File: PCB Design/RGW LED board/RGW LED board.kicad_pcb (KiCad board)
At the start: 2 copper layers, 148.6 x 22 mm, 13 parts, among them J1 R strip, J10 G strip, J11 W strip, J12 R strip, J13 G strip, J2 G strip, J3 R from above, J4 W strip, J5 G from above, J6 W from above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

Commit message: Zachary IR and RGW LED boards revisions
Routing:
- net /W-: track 101.3 -> 98.7 mm
- net /G+: track 156.5 -> 158.7 mm
- net /R+: track 155.4 -> 153.6 mm

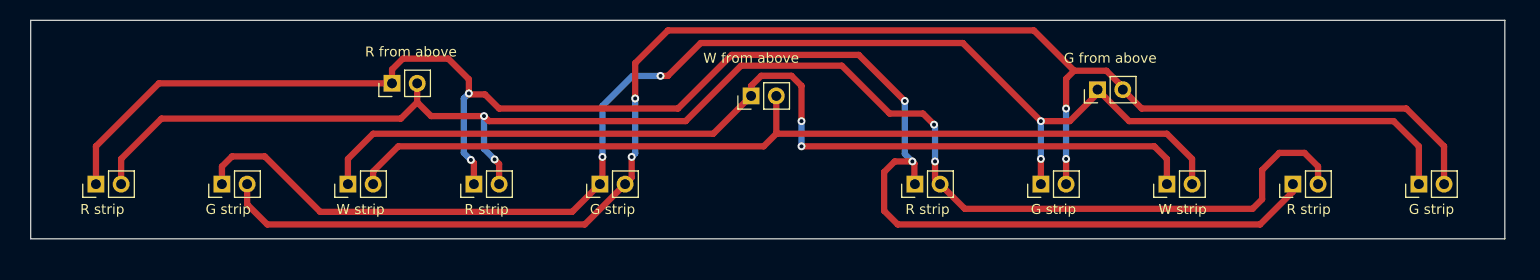
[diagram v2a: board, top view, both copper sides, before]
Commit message: Logos and labels
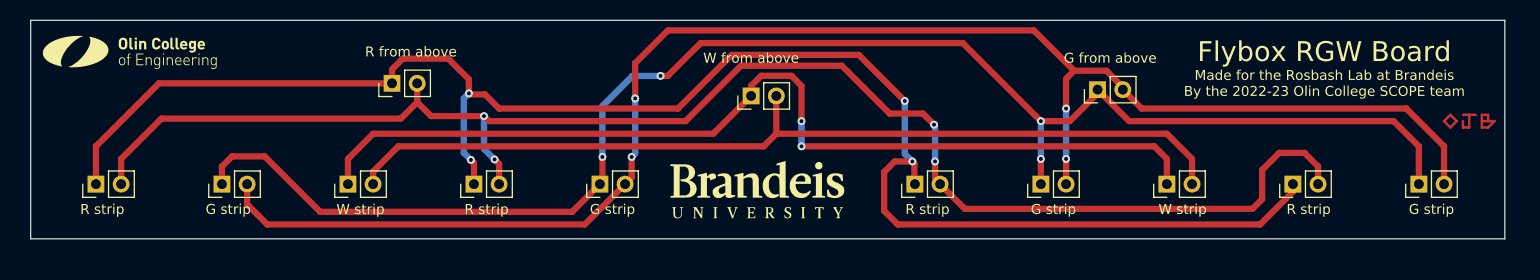
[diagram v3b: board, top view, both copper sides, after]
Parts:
- added G***: LOGO, LOGO, F.Cu at (136.5, 43.8)
- added G***: LOGO, LOGO, F.Cu at (73.0, 29.8)
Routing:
- net (no net): track 0.00 -> 12.7 mm
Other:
- board text added: "Flybox RGW Board"
- board text added: "Made for the Rosbash Lab at Brandeis By the 2022-23 Olin College SCOPE team"

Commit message: V2 IR and RGW boards done
Main board missing button footprint
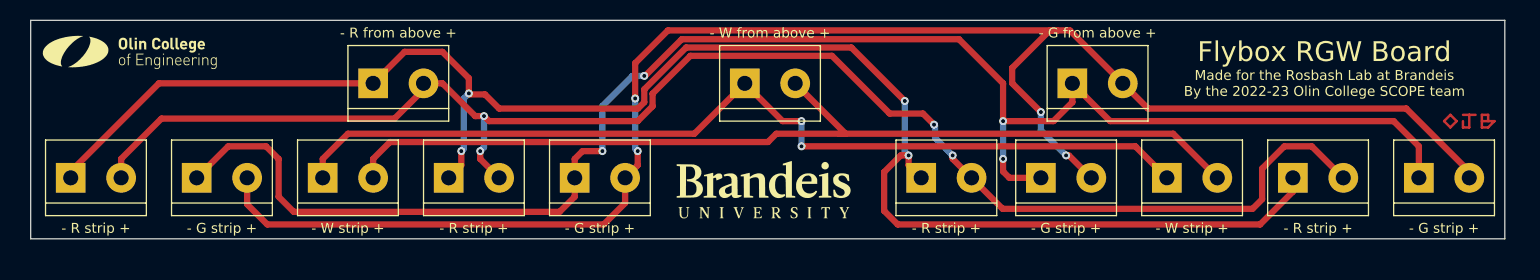
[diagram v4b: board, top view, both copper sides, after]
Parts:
- J1, J12, J7, J9: value R strip -> - R strip +; footprint Connector_PinHeader_2.54mm:PinHeader_1x02_P2.54mm_Vertical -> TerminalBlock:TerminalBlock_bornier-2_P5.08mm
- J10, J13, J2, J8: value G strip -> - G strip +; footprint Connector_PinHeader_2.54mm:PinHeader_1x02_P2.54mm_Vertical -> TerminalBlock:TerminalBlock_bornier-2_P5.08mm
- J11, J4: value W strip -> - W strip +; footprint Connector_PinHeader_2.54mm:PinHeader_1x02_P2.54mm_Vertical -> TerminalBlock:TerminalBlock_bornier-2_P5.08mm
- J3: value R from above -> - R from above +; footprint Connector_PinHeader_2.54mm:PinHeader_1x02_P2.54mm_Vertical -> TerminalBlock:TerminalBlock_bornier-2_P5.08mm
- J5: value G from above -> - G from above +; footprint Connector_PinHeader_2.54mm:PinHeader_1x02_P2.54mm_Vertical -> TerminalBlock:TerminalBlock_bornier-2_P5.08mm
- J6: value W from above -> - W from above +; footprint Connector_PinHeader_2.54mm:PinHeader_1x02_P2.54mm_Vertical -> TerminalBlock:TerminalBlock_bornier-2_P5.08mm
- moved J1 2.62 mm to (105.4, 42.5), turned to 0 degrees
- moved J10 2.62 mm to (118.1, 42.5), turned to 0 degrees
- moved J11 2.62 mm to (92.7, 42.5), turned to 0 degrees
- moved J13 2.62 mm to (80.0, 42.5), turned to 0 degrees
- moved J5 2.62 mm to (168.3, 33.0), turned to 0 degrees
- moved J9 2.62 mm to (67.3, 42.5), turned to 0 degrees
- moved J3 1.90 mm to (97.8, 33.0), turned to 0 degrees
- moved J6 1.42 mm to (135.3, 33.0), turned to 0 degrees
- moved J7 0.90 mm to (153.0, 42.5), turned to 0 degrees
- moved J12 0.63 mm to (190.5, 42.5), turned to 0 degrees
- moved J2 0.63 mm to (203.2, 42.5), turned to 0 degrees
- moved J4 0.63 mm to (177.8, 42.5), turned to 0 degrees
- moved J8 0.63 mm to (165.1, 42.5), turned to 0 degrees
- moved G*** 0.63 mm to (137.2, 43.8)
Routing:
- net /G+: track 158.7 -> 169.9 mm
- net /G-: track 154.0 -> 164.9 mm
- net /W+: track 92.8 -> 97.7 mm
- net /W-: track 98.7 -> 95.6 mm
- net /R-: track 166.7 -> 167.9 mm

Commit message: Finished V2 PCBs with rounded edges
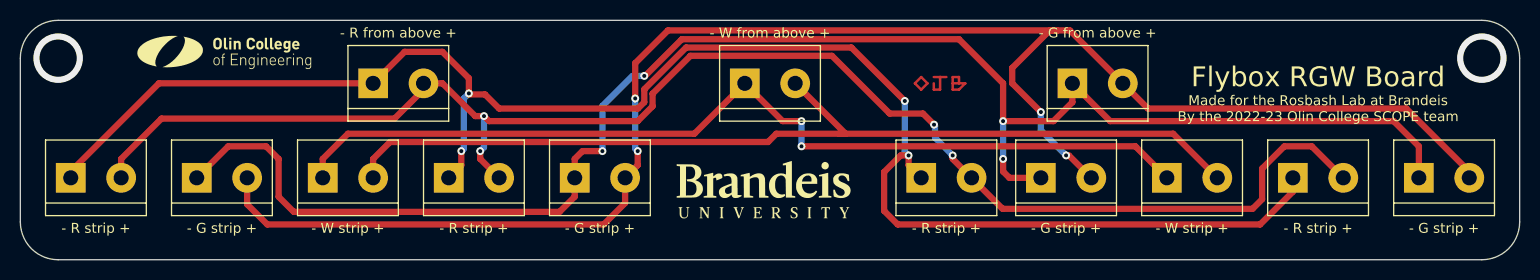
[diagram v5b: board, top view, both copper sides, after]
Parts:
- moved G*** 9.52 mm to (82.5, 29.8)
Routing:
- net (no net): vias 0 -> 2
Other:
- board size 148.6 x 22 mm -> 151.1 x 24.1 mm
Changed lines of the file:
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@@
   )
   (footprint "LOGO" (layer "F.Cu")
-    (at 73.025 29.845)
+    (at 82.55 29.845)
     (attr board_only exclude_from_pos_files exclude_from_bom)
     (fp_text reference "G***" (at 0 -1.905) (layer "F.Fab")
@@
     )
   )
-  (gr_rect (start 63.2714 26.67) (end 211.8614 48.6918) (layer "Edge.Cuts") (width 0.1) (fill none))
-  (gr_text "Made for the Rosbash Lab at Brandeis\nBy the 2022-23 Olin College SCOPE team" (at 193.675 33.02) (layer "F.SilkS")
+  (gr_arc (start 62.23 30.48) (mid 63.345923 27.785923) (end 66.04 26.67) (layer "Edge.Cuts") (width 0.1))
+  (gr_line (start 66.04 50.8) (end 209.55 50.8) (layer "Edge.Cuts") (width 0.1))
+  (gr_line (start 209.55 26.67) (end 66.04 26.67) (layer "Edge.Cuts") (width 0.1))
+  (gr_arc (start 209.55 26.67) (mid 212.244077 27.785923) (end 213.36 30.48) (layer "Edge.Cuts") (width 0.1))
+  (gr_arc (start 66.04 50.8) (mid 63.345923 49.684077) (end 62.23 46.99) (layer "Edge.Cuts") (width 0.1))
+  (gr_line (start 62.23 30.48) (end 62.23 46.99) (layer "Edge.Cuts") (width 0.1))
+  (gr_line (start 213.36 46.99) (end 213.36 30.48) (layer "Edge.Cuts") (width 0.1))
+  (gr_arc (start 213.36 46.99) (mid 212.244077 49.684077) (end 209.55 50.8) (layer "Edge.Cuts") (width 0.1))
+  (gr_rect (start 62.23 26.67) (end 213.36 50.8) (layer "F.Fab") (width 0.1) (fill none))
+  (gr_text "Made for the Rosbash Lab at Brandeis\nBy the 2022-23 Olin College SCOPE team" (at 193.04 35.56) (layer "F.SilkS")
     (effects (font (size 1 1) (thickness 0.2)))
   )
-  (gr_text "Flybox RGW Board\n" (at 193.675 29.845) (layer "F.SilkS")
+  (gr_text "Flybox RGW Board\n" (at 193.04 32.385) (layer "F.SilkS")
     (effects (font (size 2 2) (thickness 0.2)))
   )
-  (segment (start 210.82 36.83) (end 209.55 36.83) (width 0.25) (layer "F.Cu") (net 0))
-  (segment (start 210.185 36.195) (end 210.185 36.83) (width 0.25) (layer "F.Cu") (net 0))
-  (segment (start 207.645 36.195) (end 208.28 36.195) (width 0.25) (layer "F.Cu") (net 0))
-  (segment (start 209.55 36.195) (end 209.55 37.465) (width 0.25) (layer "F.Cu") (net 0))
-  (segment (start 207.01 36.83) (end 206.375 37.465) (width 0.25) (layer "F.Cu") (net 0))
-  (segment (start 205.74 36.83) (end 206.375 36.195) (width 0.25) (layer "F.Cu") (net 0))
-  (segment (start 207.645 37.465) (end 207.645 36.83) (width 0.25) (layer "F.Cu") (net 0))
-  (segment (start 209.55 37.465) (end 210.185 37.465) (width 0.25) (layer "F.Cu") (net 0))
-  (segment (start 206.375 36.195) (end 207.01 36.83) (width 0.25) (layer "F.Cu") (net 0))
-  (segment (start 210.185 37.465) (end 210.82 36.83) (width 0.25) (layer "F.Cu") (net 0))
-  (segment (start 208.28 36.195) (end 208.28 37.465) (width 0.25) (layer "F.Cu") (net 0))
-  (segment (start 209.55 36.195) (end 210.185 36.195) (width 0.25) (layer "F.Cu") (net 0))
-  (segment (start 206.375 37.465) (end 205.74 36.83) (width 0.25) (layer "F.Cu") (net 0))
-  (segment (start 208.28 37.465) (end 207.645 37.465) (width 0.25) (layer "F.Cu") (net 0))
-  (segment (start 208.28 36.195) (end 208.915 36.195) (width 0.25) (layer "F.Cu") (net 0))
+  (segment (start 157.48 33.02) (end 156.21 33.02) (width 0.25) (layer "F.Cu") (net 0))
+  (segment (start 156.845 32.385) (end 156.845 33.02) (width 0.25) (layer "F.Cu") (net 0))
+  (segment (start 154.305 32.385) (end 154.94 32.385) (width 0.25) (layer "F.Cu") (net 0))
+  (segment (start 156.21 32.385) (end 156.21 33.655) (width 0.25) (layer "F.Cu") (net 0))
+  (segment (start 153.67 33.02) (end 153.035 33.655) (width 0.25) (layer "F.Cu") (net 0))
+  (segment (start 152.4 33.02) (end 153.035 32.385) (width 0.25) (layer "F.Cu") (net 0))
+  (segment (start 154.305 33.655) (end 154.305 33.02) (width 0.25) (layer "F.Cu") (net 0))
+  (segment (start 156.21 33.655) (end 156.845 33.655) (width 0.25) (layer "F.Cu") (net 0))
+  (segment (start 153.035 32.385) (end 153.67 33.02) (width 0.25) (layer "F.Cu") (net 0))
+  (segment (start 156.845 33.655) (end 157.48 33.02) (width 0.25) (layer "F.Cu") (net 0))
+  (segment (start 154.94 32.385) (end 154.94 33.655) (width 0.25) (layer "F.Cu") (net 0))
+  (segment (start 156.21 32.385) (end 156.845 32.385) (width 0.25) (layer "F.Cu") (net 0))
+  (segment (start 153.035 33.655) (end 152.4 33.02) (width 0.25) (layer "F.Cu") (net 0))
+  (segment (start 154.94 33.655) (end 154.305 33.655) (width 0.25) (layer "F.Cu") (net 0))
+  (segment (start 154.94 32.385) (end 155.575 32.385) (width 0.25) (layer "F.Cu") (net 0))
+  (via (at 66.04 30.48) (size 5) (drill 3.75) (layers "F.Cu" "B.Cu") (free) (net 0))
+  (via (at 209.55 30.48) (size 5) (drill 3.75) (layers "F.Cu" "B.Cu") (free) (net 0))
   (segment (start 100.965 29.845) (end 104.775 29.845) (width 0.635) (layer "F.Cu") (net 1))
   (segment (start 97.79 33.02) (end 76.2 33.02) (width 0.635) (layer "F.Cu") (net 1))

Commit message: Shrunk vias, fixed ohms and XV1 labels
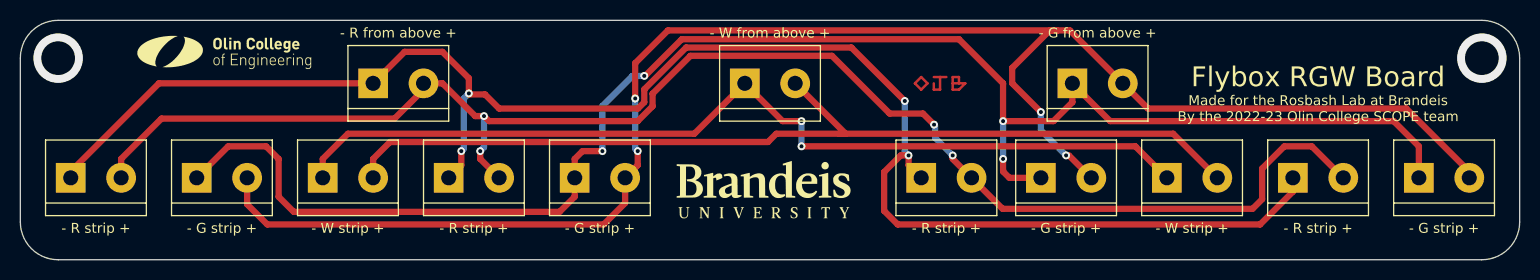
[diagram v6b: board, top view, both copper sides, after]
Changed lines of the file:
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@@
   (segment (start 154.94 33.655) (end 154.305 33.655) (width 0.25) (layer "F.Cu") (net 0))
   (segment (start 154.94 32.385) (end 155.575 32.385) (width 0.25) (layer "F.Cu") (net 0))
-  (via (at 66.04 30.48) (size 5) (drill 3.75) (layers "F.Cu" "B.Cu") (free) (net 0))
-  (via (at 209.55 30.48) (size 5) (drill 3.75) (layers "F.Cu" "B.Cu") (free) (net 0))
+  (via (at 66.04 30.48) (size 5) (drill 3.4) (layers "F.Cu" "B.Cu") (free) (net 0))
+  (via (at 209.55 30.48) (size 5) (drill 3.4) (layers "F.Cu" "B.Cu") (free) (net 0))
   (segment (start 100.965 29.845) (end 104.775 29.845) (width 0.635) (layer "F.Cu") (net 1))
   (segment (start 97.79 33.02) (end 76.2 33.02) (width 0.635) (layer "F.Cu") (net 1))

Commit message: Zachary review of IR and RGW and Fans boards
@oliviajobradley All done reviewing all three boards. I played with the silkscreen a bit, not sure if it's better or worse. OJ, feel free to change it back if you'd prefer.

Let's order!
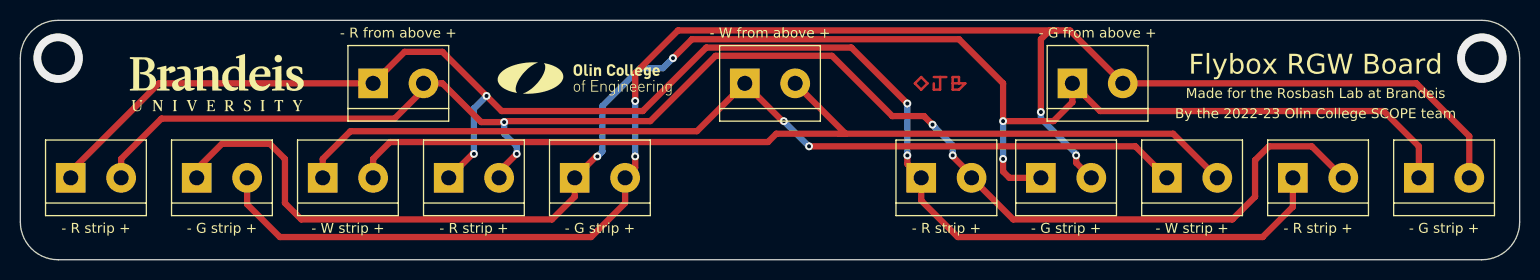
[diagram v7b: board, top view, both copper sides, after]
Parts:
- moved G*** 56.2 mm to (82.0, 33.0)
- moved G*** 36.4 mm to (118.9, 32.5)
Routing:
- net /R-: track 167.9 -> 160.9 mm
- net /W-: track 95.6 -> 94.1 mm
- net /G-: track 164.9 -> 165.5 mm
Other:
- board text added: "By the 2022-23 Olin College SCOPE team"
- board text added: "Made for the Rosbash Lab at Brandeis"
- board text removed: "Made for the Rosbash Lab at Brandeis By the 2022-23 Olin College SCOPE team"
